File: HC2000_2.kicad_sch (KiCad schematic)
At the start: 37 parts, among them T1 BD139

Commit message: Updated ICs values and positions
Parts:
- UB6: value ROM - 27C256 -> 27C256/27C512
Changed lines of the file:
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@@
       (effects (font (size 1.778 1.5113)) (justify left bottom))
     )
-    (property "Value" "ROM - 27C256" (at 149.86 86.36 0)
+    (property "Value" "27C256/27C512" (at 149.86 86.36 0)
       (effects (font (size 1.778 1.5113)) (justify left bottom))
     )

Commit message: Fix errors (IC & unnoticed cut for 1 EPROM)
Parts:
- UA23, UA34: value 7409N -> 74LS09
- UB3: value 74367N -> 74LS367
- UC1: value 7404N -> 74LS04
- UC6: value 74373N -> 74LS373
- UE3: value 7432N -> 74LS32
- UE4: value 74138N -> 74LS138
- UF7: value 74174N -> 74LS174
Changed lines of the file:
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@@
       (effects (font (size 1.778 1.5113)) (justify left bottom))
     )
-    (property "Value" "7432N" (at 205.74 193.04 0)
+    (property "Value" "74LS32" (at 205.74 193.04 0)
       (effects (font (size 1.778 1.5113)) (justify left bottom))
     )
@@
       (effects (font (size 1.778 1.5113)) (justify left bottom))
     )
-    (property "Value" "74174N" (at 149.86 190.5 0)
+    (property "Value" "74LS174" (at 149.86 190.5 0)
       (effects (font (size 1.778 1.5113)) (justify left bottom))
     )
@@
       (effects (font (size 1.778 1.5113)) (justify left bottom))
     )
-    (property "Value" "7409N" (at 241.3 40.64 0)
+    (property "Value" "74LS09" (at 241.3 40.64 0)
       (effects (font (size 1.778 1.5113)) (justify left bottom))
     )
@@
       (effects (font (size 1.778 1.5113)) (justify left bottom))
     )
-    (property "Value" "74138N" (at 43.18 142.24 0)
+    (property "Value" "74LS138" (at 43.18 142.24 0)
       (effects (font (size 1.778 1.5113)) (justify left bottom))
     )
@@
       (effects (font (size 1.778 1.5113)) (justify left bottom))
     )
-    (property "Value" "7404N" (at 213.36 165.1 0)
+    (property "Value" "74LS04" (at 213.36 165.1 0)
       (effects (font (size 1.778 1.5113)) (justify left bottom))
     )
@@
       (effects (font (size 1.778 1.5113)) (justify left bottom))
     )
-    (property "Value" "7409N" (at 241.3 93.98 0)
+    (property "Value" "74LS09" (at 241.3 93.98 0)
       (effects (font (size 1.778 1.5113)) (justify left bottom))
     )
@@
       (effects (font (size 1.778 1.5113)) (justify left bottom))
     )
-    (property "Value" "7409N" (at 241.3 129.54 0)
+    (property "Value" "74LS09" (at 241.3 129.54 0)
       (effects (font (size 1.778 1.5113)) (justify left bottom))
     )
@@
       (effects (font (size 1.778 1.5113)) (justify left bottom))
     )
-    (property "Value" "74373N" (at 241.3 203.2 0)
+    (property "Value" "74LS373" (at 241.3 203.2 0)
       (effects (font (size 1.778 1.5113)) (justify left bottom))
     )
@@
       (effects (font (size 1.778 1.5113)) (justify left bottom))
     )
-    (property "Value" "7409N" (at 241.3 165.1 0)
+    (property "Value" "74LS09" (at 241.3 165.1 0)
       (effects (font (size 1.778 1.5113)) (justify left bottom))
     )
@@
       (effects (font (size 1.778 1.5113)) (justify left bottom))
     )
-    (property "Value" "7409N" (at 241.3 58.42 0)
+    (property "Value" "74LS09" (at 241.3 58.42 0)
       (effects (font (size 1.778 1.5113)) (justify left bottom))
     )
@@
       (effects (font (size 1.778 1.5113)) (justify left bottom))
     )
-    (property "Value" "7404N" (at 96.52 180.34 0)
+    (property "Value" "74LS04" (at 96.52 180.34 0)
       (effects (font (size 1.778 1.5113)) (justify left bottom))
     )
@@
       (effects (font (size 1.778 1.5113)) (justify left bottom))
     )
-    (property "Value" "7409N" (at 241.3 76.2 0)
+    (property "Value" "74LS09" (at 241.3 76.2 0)
       (effects (font (size 1.778 1.5113)) (justify left bottom))
     )
@@
       (effects (font (size 1.778 1.5113)) (justify left bottom))
     )
-    (property "Value" "7409N" (at 241.3 111.76 0)
+    (property "Value" "74LS09" (at 241.3 111.76 0)
       (effects (font (size 1.778 1.5113)) (justify left bottom))
     )
@@
       (effects (font (size 1.778 1.5113)) (justify left bottom))
     )
-    (property "Value" "74367N" (at 149.86 157.48 0)
+    (property "Value" "74LS367" (at 149.86 157.48 0)
       (effects (font (size 1.778 1.5113)) (justify left bottom))
     )
@@
       (effects (font (size 1.778 1.5113)) (justify left bottom))
     )
-    (property "Value" "7409N" (at 241.3 147.32 0)
-      (effects (font (size 1.778 1.5113)) (justify left bottom))
-    )
+    (property "Value" "74LS09" (at 241.3 147.32 0)
+      (effects (font (size 1.778 1.5113)) (justify left bottom))
+    )

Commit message: Revision-E
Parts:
- R5, R60: value 330/300 -> 300
- UB6: value 27C256/27C512 -> 27C512
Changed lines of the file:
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@@
       (effects (font (size 1.778 1.5113)) (justify left bottom))
     )
-    (property "Value" "330/300" (at 84.582 201.93 0)
+    (property "Value" "300" (at 84.582 201.93 0)
       (effects (font (size 1.778 1.5113)) (justify left bottom))
     )
@@
       (effects (font (size 1.778 1.5113)) (justify left bottom))
     )
-    (property "Value" "27C256/27C512" (at 149.86 86.36 0)
+    (property "Value" "27C512" (at 149.86 86.36 0)
       (effects (font (size 1.778 1.5113)) (justify left bottom))
     )
@@
       (effects (font (size 1.778 1.5113)) (justify left bottom))
     )
-    (property "Value" "330/300" (at 54.102 31.75 0)
-      (effects (font (size 1.778 1.5113)) (justify left bottom))
-    )
+    (property "Value" "300" (at 54.102 31.75 0)
+      (effects (font (size 1.778 1.5113)) (justify left bottom))
+    )

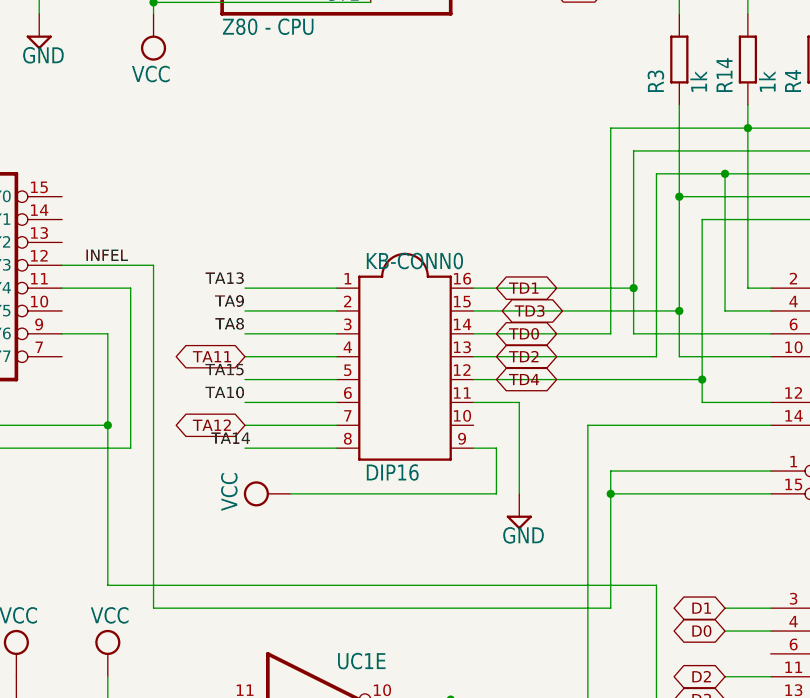
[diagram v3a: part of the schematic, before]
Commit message: Updated power, audio and keyboard connectors
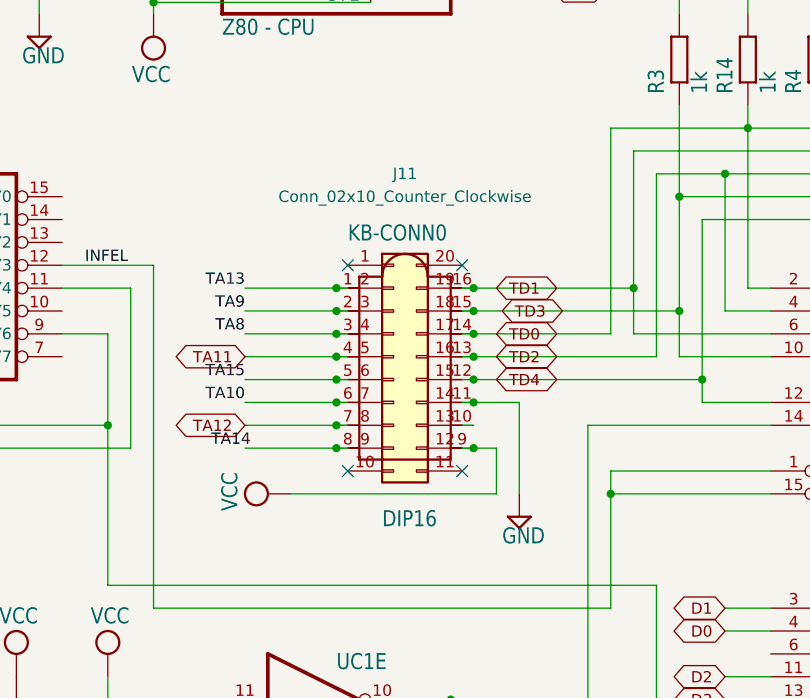
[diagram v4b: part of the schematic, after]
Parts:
- added J11: Conn_02x10_Counter_Clockwise, HC2000:PinHeader_2x10_P2.54mm_Vertical, symbol HC2000:Conn_02x10_Counter_Clockwise
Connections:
- net GND: now also J11.14 (Pin_14)
- net TA10: now also J11.7 (Pin_7)
- net TA11: now also J11.5 (Pin_5)
- net TA12: now also J11.8 (Pin_8)
- net TA13: now also J11.2 (Pin_2)
- net TA14: now also J11.9 (Pin_9)
- net TA15: now also J11.6 (Pin_6)
- net TA8: now also J11.4 (Pin_4)
- net TA9: now also J11.3 (Pin_3)
- net TD0: now also J11.17 (Pin_17)
- net TD1: now also J11.19 (Pin_19)
- net TD2: now also J11.16 (Pin_16)
- net TD3: now also J11.18 (Pin_18)
- net TD4: now also J11.15 (Pin_15)
- net VCC: now also J11.12 (Pin_12)
- net at KB-CONN0.10: now also J11.13 (Pin_13)
- no-connect marks 0 -> 4
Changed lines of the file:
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@@
   (junction (at 73.66 60.96) (diameter 0) (color 0 0 0 0)
   )
+  (junction (at 111.76 142.24) (diameter 0) (color 0 0 0 0)
+  )
   (junction (at 129.54 129.54) (diameter 0) (color 0 0 0 0)
   )
@@
   (junction (at 134.62 132.08) (diameter 0) (color 0 0 0 0)
   )
+  (junction (at 96.52 137.16) (diameter 0) (color 0 0 0 0)
+  )
   (junction (at 231.14 160.02) (diameter 0) (color 0 0 0 0)
   )
+  (junction (at 111.76 129.54) (diameter 0) (color 0 0 0 0)
+  )
   (junction (at 157.48 116.84) (diameter 0) (color 0 0 0 0)
   )
   (junction (at 81.28 187.96) (diameter 0) (color 0 0 0 0)
   )
+  (junction (at 111.76 134.62) (diameter 0) (color 0 0 0 0)
+  )
   (junction (at 50.8 20.32) (diameter 0) (color 0 0 0 0)
   )
@@
   (junction (at 73.66 20.32) (diameter 0) (color 0 0 0 0)
   )
+  (junction (at 96.52 144.78) (diameter 0) (color 0 0 0 0)
+  )
+  (junction (at 96.52 142.24) (diameter 0) (color 0 0 0 0)
+  )
   (junction (at 165.1 121.92) (diameter 0) (color 0 0 0 0)
   )
+  (junction (at 111.76 132.08) (diameter 0) (color 0 0 0 0)
+  )
+  (junction (at 96.52 139.7) (diameter 0) (color 0 0 0 0)
+  )
   (junction (at 165.1 96.52) (diameter 0) (color 0 0 0 0)
   )
+  (junction (at 96.52 134.62) (diameter 0) (color 0 0 0 0)
+  )
   (junction (at 231.14 106.68) (diameter 0) (color 0 0 0 0)
   )
   (junction (at 50.8 86.36) (diameter 0) (color 0 0 0 0)
   )
+  (junction (at 96.52 132.08) (diameter 0) (color 0 0 0 0)
+  )
   (junction (at 149.86 96.52) (diameter 0) (color 0 0 0 0)
   )
+  (junction (at 111.76 137.16) (diameter 0) (color 0 0 0 0)
+  )
+  (junction (at 111.76 139.7) (diameter 0) (color 0 0 0 0)
+  )
   (junction (at 76.2 97.79) (diameter 0) (color 0 0 0 0)
   )
@@
   (junction (at 231.14 88.9) (diameter 0) (color 0 0 0 0)
   )
+  (junction (at 96.52 147.32) (diameter 0) (color 0 0 0 0)
+  )
+  (junction (at 111.76 147.32) (diameter 0) (color 0 0 0 0)
+  )
   (junction (at 231.14 124.46) (diameter 0) (color 0 0 0 0)
   )
@@
   (junction (at 66.04 68.58) (diameter 0) (color 0 0 0 0)
   )
+  (junction (at 96.52 129.54) (diameter 0) (color 0 0 0 0)
+  )
   (junction (at 109.22 175.26) (diameter 0) (color 0 0 0 0)
   )
@@
   (junction (at 157.48 96.52) (diameter 0) (color 0 0 0 0)
   )
+  (no_connect (at 110.49 149.86))
+  (no_connect (at 97.79 149.86))
+  (no_connect (at 110.49 127))
+  (no_connect (at 97.79 127))
   (wire (pts (xy 109.22 190.5) (xy 109.22 193.04))
     (stroke (width 0) (type default))
@@
     (stroke (width 0) (type default))
   )
+  (wire (pts (xy 96.52 147.32) (xy 97.79 147.32))
+    (stroke (width 0) (type default))
+  )
   (wire (pts (xy 137.16 139.7) (xy 111.76 139.7))
     (stroke (width 0) (type default))
@@
     (stroke (width 0) (type default))
   )
+  (wire (pts (xy 110.49 142.24) (xy 111.76 142.24))
+    (stroke (width 0) (type default))
+  )
   (wire (pts (xy 142.24 187.96) (xy 142.24 185.42))
     (stroke (width 0) (type default))
@@
     (stroke (width 0) (type default))
   )
+  (wire (pts (xy 96.52 137.16) (xy 97.79 137.16))
+    (stroke (width 0) (type default))
+  )
   (wire (pts (xy 43.18 99.06) (xy 43.18 73.66))
     (stroke (width 0) (type default))
@@
     (stroke (width 0) (type default))
   )
+  (wire (pts (xy 110.49 139.7) (xy 111.76 139.7))
+    (stroke (width 0) (type default))
+  )
   (wire (pts (xy 182.88 116.84) (xy 157.48 116.84))
     (stroke (width 0) (type default))
@@
     (stroke (width 0) (type default))
   )
+  (wire (pts (xy 110.49 132.08) (xy 111.76 132.08))
+    (stroke (width 0) (type default))
+  )
   (wire (pts (xy 27.94 78.74) (xy 58.42 78.74))
     (stroke (width 0) (type default))
@@
     (stroke (width 0) (type default))
   )
+  (wire (pts (xy 110.49 144.78) (xy 111.76 144.78))
+    (stroke (width 0) (type default))
+  )
   (wire (pts (xy 236.22 106.68) (xy 231.14 106.68))
     (stroke (width 0) (type default))
@@
     (stroke (width 0) (type default))
   )
+  (wire (pts (xy 110.49 147.32) (xy 111.76 147.32))
+    (stroke (width 0) (type default))
+  )
   (wire (pts (xy 236.22 160.02) (xy 231.14 160.02))
     (stroke (width 0) (type default))
@@
     (stroke (width 0) (type default))
   )
+  (wire (pts (xy 96.52 134.62) (xy 97.79 134.62))
+    (stroke (width 0) (type default))
+  )
   (wire (pts (xy 220.98 160.02) (xy 231.14 160.02))
     (stroke (width 0) (type default))
@@
     (stroke (width 0) (type default))
   )
+  (wire (pts (xy 110.49 134.62) (xy 111.76 134.62))
+    (stroke (width 0) (type default))
+  )
   (wire (pts (xy 127 165.1) (xy 127 152.4))
     (stroke (width 0) (type default))
@@
     (stroke (width 0) (type default))
   )
+  (wire (pts (xy 96.52 139.7) (xy 97.79 139.7))
+    (stroke (width 0) (type default))
+  )
   (wire (pts (xy 182.88 172.72) (xy 170.18 172.72))
     (stroke (width 0) (type default))
@@
     (stroke (width 0) (type default))
   )
+  (wire (pts (xy 96.52 132.08) (xy 97.79 132.08))
+    (stroke (width 0) (type default))
+  )
   (wire (pts (xy 120.65 96.52) (xy 114.3 96.52))
     (stroke (width 0) (type default))
@@
     (stroke (width 0) (type default))
   )
+  (wire (pts (xy 96.52 129.54) (xy 97.79 129.54))
+    (stroke (width 0) (type default))
+  )
   (wire (pts (xy 120.65 93.98) (xy 114.3 93.98))
     (stroke (width 0) (type default))
@@
     (stroke (width 0) (type default))
   )
+  (wire (pts (xy 96.52 144.78) (xy 97.79 144.78))
+    (stroke (width 0) (type default))
+  )
   (wire (pts (xy 172.72 190.5) (xy 172.72 193.04))
     (stroke (width 0) (type default))
@@
     (stroke (width 0) (type default))
   )
+  (wire (pts (xy 110.49 137.16) (xy 111.76 137.16))
+    (stroke (width 0) (type default))
+  )
   (wire (pts (xy 71.12 134.62) (xy 66.04 134.62))
     (stroke (width 0) (type default))
@@
     (stroke (width 0) (type default))
   )
+  (wire (pts (xy 110.49 129.54) (xy 111.76 129.54))
+    (stroke (width 0) (type default))
+  )
   (wire (pts (xy 27.94 152.4) (xy 38.1 152.4))
     (stroke (width 0) (type default))
@@
     (stroke (width 0) (type default))
   )
+  (wire (pts (xy 96.52 142.24) (xy 97.79 142.24))
+    (stroke (width 0) (type default))
+  )
   (wire (pts (xy 73.66 22.86) (xy 73.66 20.32))
     (stroke (width 0) (type default))
@@
   (symbol (lib_id "HC2000:DIL16") (at 104.14 137.16 0) (unit 1)
     (in_bom yes) (on_board yes) (dnp no)
-    (property "Reference" "KB-CONN0" (at 99.695 127.635 0)
+    (property "Reference" "KB-CONN0" (at 97.79 124.46 0)
       (effects (font (size 1.778 1.5113)) (justify left bottom))
     )
-    (property "Value" "DIP16" (at 99.695 151.13 0)
+    (property "Value" "DIP16" (at 101.6 156.21 0)
       (effects (font (size 1.778 1.5113)) (justify left bottom))
     )
@@
         )
       )
+    )
+  )
+  (symbol (lib_id "HC2000:Conn_02x10_Counter_Clockwise") (at 102.87 137.16 0) (unit 1)
+    (in_bom yes) (on_board yes) (dnp no)
+    (property "Reference" "J11" (at 104.14 116.84 0)
+      (effects (font (size 1.27 1.27)))
+    )
+    (property "Value" "Conn_02x10_Counter_Clockwise" (at 104.14 119.38 0)
+      (effects (font (size 1.27 1.27)))
+    )
+    (property "Footprint" "HC2000:PinHeader_2x10_P2.54mm_Vertical" (at 102.87 137.16 0)
+      (effects (font (size 1.27 1.27)) hide)
+    )
+    (property "Datasheet" "~" (at 102.87 137.16 0)
+      (effects (font (size 1.27 1.27)) hide)
+    )
+    (pin "1")
+    (pin "10")
+    (pin "11")
+    (pin "12")
+    (pin "13")
+    (pin "14")
+    (pin "15")
+    (pin "16")
+    (pin "17")
+    (pin "18")
+    (pin "19")
+    (pin "2")
+    (pin "20")
+    (pin "3")
+    (pin "4")
+    (pin "5")
+    (pin "6")
+    (pin "7")
+    (pin "8")
+    (pin "9")
+    (instances
+      (project "HC2000"
+        (path "/2dfd2155-e8d4-4a1e-b6a1-e213718e2264/6e4e82a1-9760-425d-9311-184e3038a6b6"
+          (reference "J11") (unit 1)
+        )
+      )
